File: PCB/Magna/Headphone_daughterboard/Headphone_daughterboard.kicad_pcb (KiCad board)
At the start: 2 copper layers, 84 x 50 mm, 47 parts, among them J101 Conn_02x05_Odd_Even, J102 AudioJack3, U101 NE5532, U102 NE5532, U103 TDA2822D

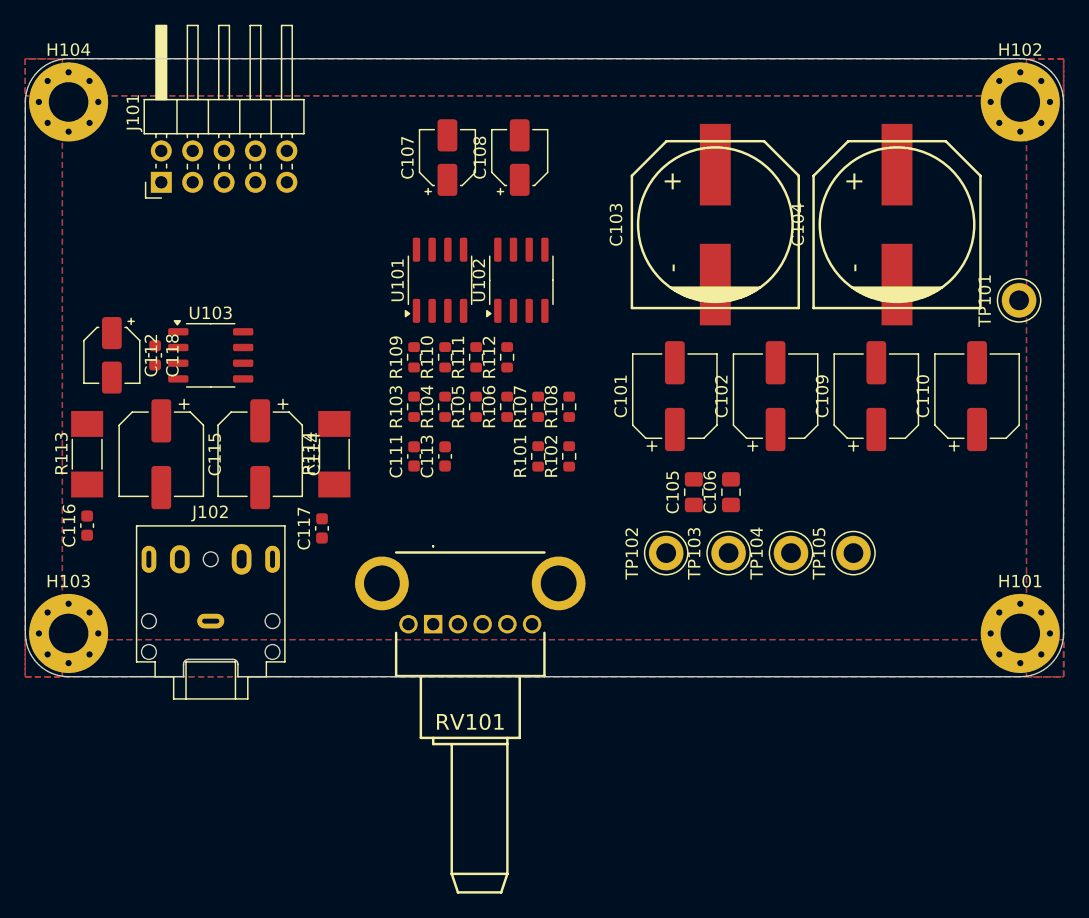
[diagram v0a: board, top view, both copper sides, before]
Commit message: Fix board alignments and mounting holes
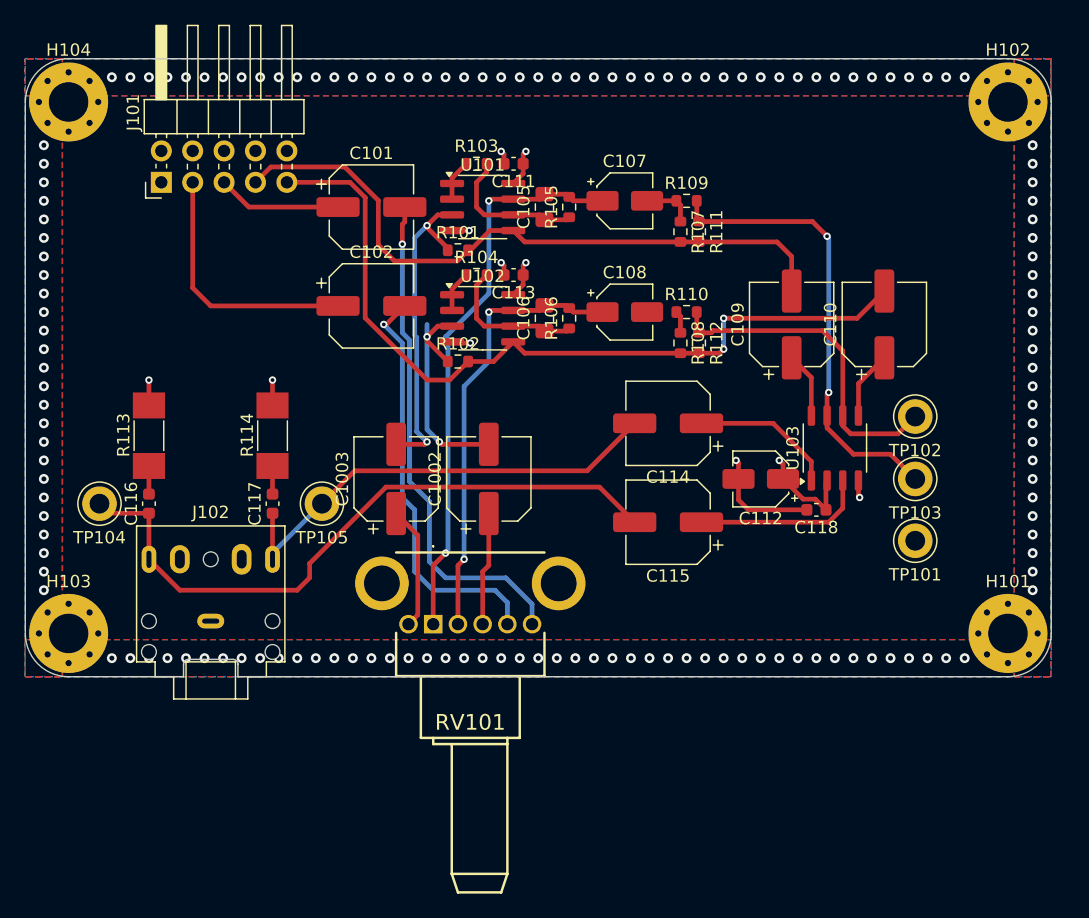
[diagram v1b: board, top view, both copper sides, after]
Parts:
- removed C103, C104: 22uF, Skrooter_footprints:c_elec_SMD_12.5x13.5
- added C1002: 22uF, Capacitor_SMD:CP_Elec_6.3x5.4, F.Cu at (108.5, 92.0)
- added C1003: 22uF, Capacitor_SMD:CP_Elec_6.3x5.4, F.Cu at (101.0, 92.0)
- moved TP104 56.1 mm to (77.0, 94.0), turned to 180 degrees
- moved C118 54.9 mm to (135.0, 94.5), turned to 180 degrees
- moved C112 53.4 mm to (130.5, 92.0), turned to 180 degrees
- moved U103 51.1 mm to (136.5, 89.5), turned to 90 degrees
- moved TP105 43.2 mm to (95.0, 94.0), turned to 180 degrees
- moved C115 41.4 mm to (123.0, 95.5), turned to 180 degrees
- moved C102 33.5 mm to (99.0, 78.0), turned to 0 degrees
- moved C114 33.1 mm to (123.0, 87.5), turned to 180 degrees
- moved C101 28.9 mm to (99.0, 70.0), turned to 0 degrees
- moved C105 26.0 mm to (113.0, 70.0)
- moved R109 25.4 mm to (124.5, 69.5), turned to 0 degrees
- moved C111 25.0 mm to (110.5, 66.5), turned to 180 degrees
- moved TP102 23.0 mm to (143.0, 87.0), turned to 180 degrees
- moved TP101 21.2 mm to (143.0, 97.0), turned to 180 degrees
- moved R111 20.7 mm to (125.5, 72.0), turned to -90 degrees
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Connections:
- J101 pad 3: /AudioInL -> /AudioInR
- J101 pad 5: /AudioInR -> /AudioInL
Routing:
- net /VAA_BIAS_R: track 0.00 -> 65.9 mm, vias 0 -> 2
- net Net-(C115-Pad2): track 0.00 -> 53.7 mm
- net /VAA_BIAS_L: track 0.00 -> 53.7 mm
- net Net-(C105-Pad2): track 0.00 -> 45.9 mm, vias 0 -> 2
- net Net-(C101-Pad2): track 0.00 -> 41.0 mm, vias 0 -> 1
- net Net-(C114-Pad2): track 0.00 -> 37.9 mm
- net Net-(U103-Input1-): track 0.00 -> 37.1 mm, vias 0 -> 2
- net Net-(C106-Pad2): track 0.00 -> 35.9 mm, vias 0 -> 2
- net Net-(C102-Pad2): track 0.00 -> 33.6 mm, vias 0 -> 1
- net Net-(U103-Input2-): track 0.00 -> 26.9 mm
- net Net-(U101A-+): track 0.00 -> 25.8 mm, vias 0 -> 2
- net /AudioInR: track 0.00 -> 20.9 mm
- net GND: track 0.00 -> 19.7 mm, vias 0 -> 8
- net Net-(U102A-+): track 0.00 -> 19.1 mm, vias 0 -> 2
- net Net-(U103-OUTPUT2): track 0.00 -> 14.4 mm
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- added copper zone on In1.Cu, net GND
- added copper zone on In2.Cu, net GND
- added copper zone on In1.Cu, net SHIELD
- added copper zone on In2.Cu, net SHIELD
- added copper zone on B.Cu, net VAA
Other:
- board size 84 x 50 mm -> 83 x 50 mm
- copper layers 2 -> 4
